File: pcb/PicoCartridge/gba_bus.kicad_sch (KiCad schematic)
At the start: 1 part, among them J1 GameBoy_GamePak_AGB-002

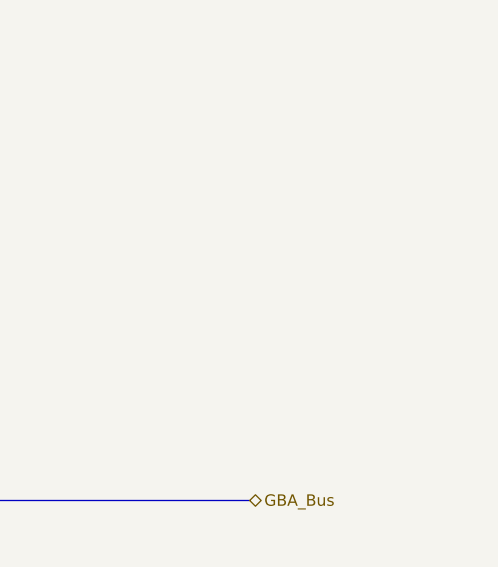
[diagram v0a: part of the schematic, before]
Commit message: Defined additional interfaces
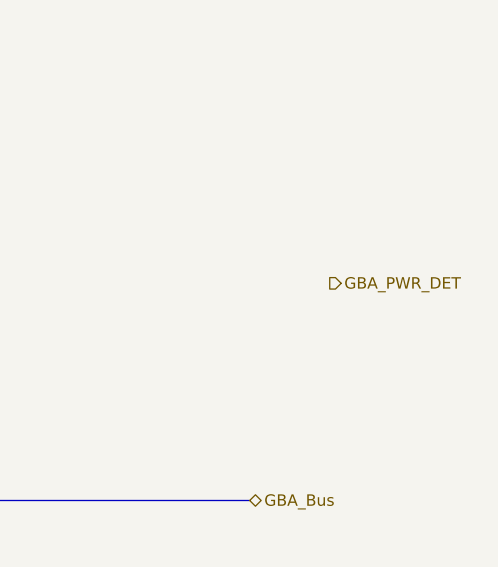
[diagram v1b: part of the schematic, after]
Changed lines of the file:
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@@
+		)
+	)
+	(hierarchical_label "GBA_PWR_DET"
+		(shape output)
+		(at 127 96.52 0)
+		(fields_autoplaced yes)
+		(effects
+			(font
+				(size 1.27 1.27)
+			)
+			(justify left)
 		)
 	)

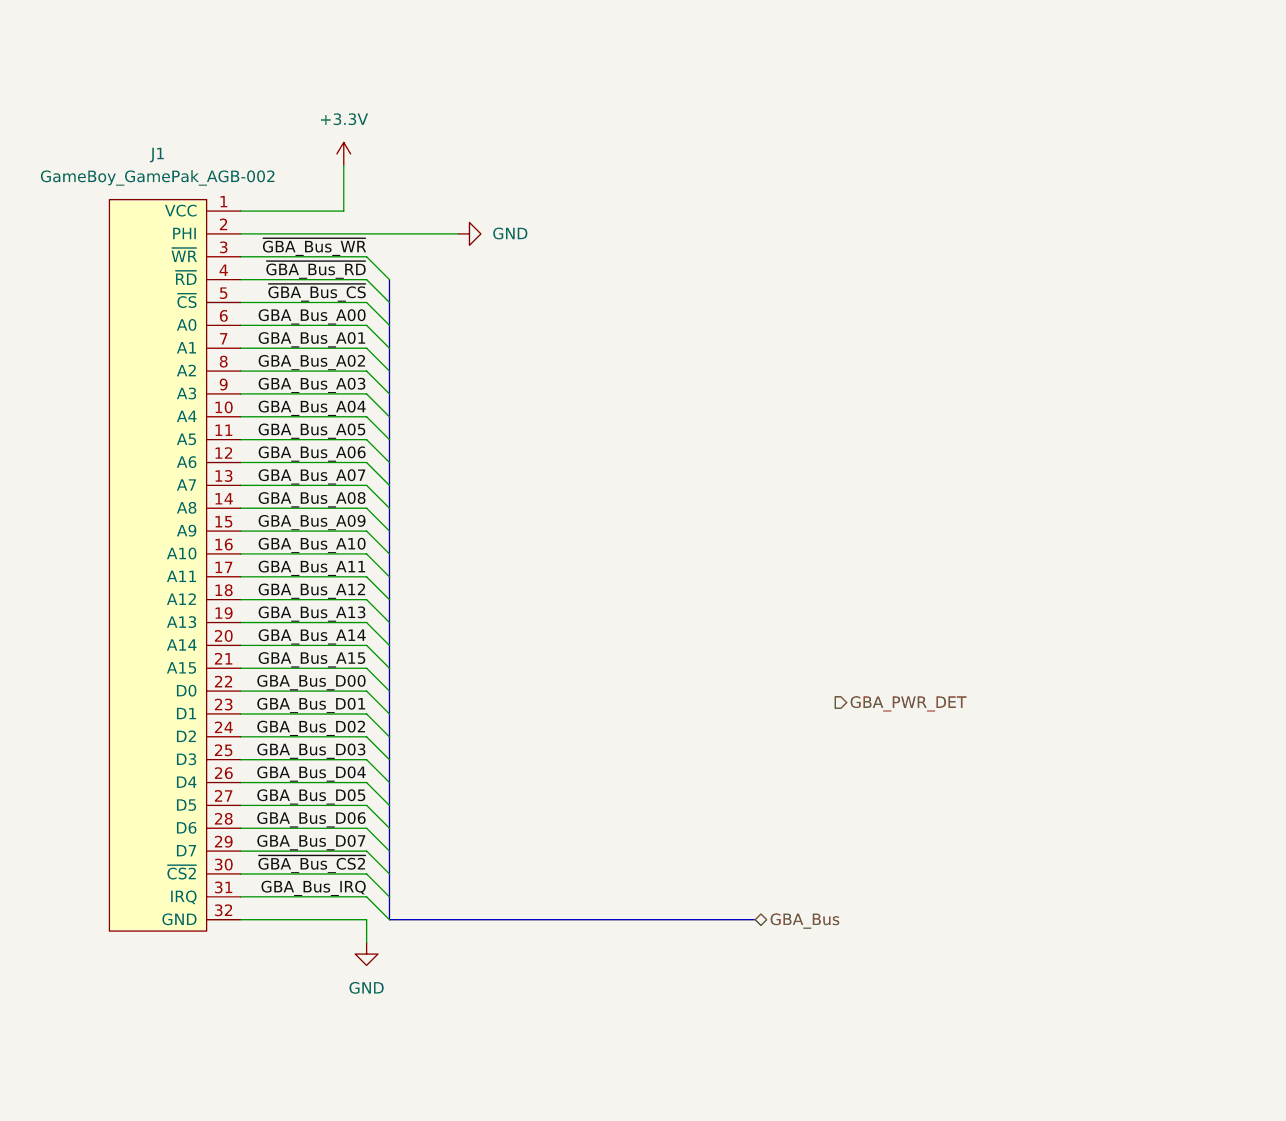
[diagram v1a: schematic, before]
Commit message: Fixed GBA bus internal logic
THe GBA bus is now a correct bus in a sense of kicad
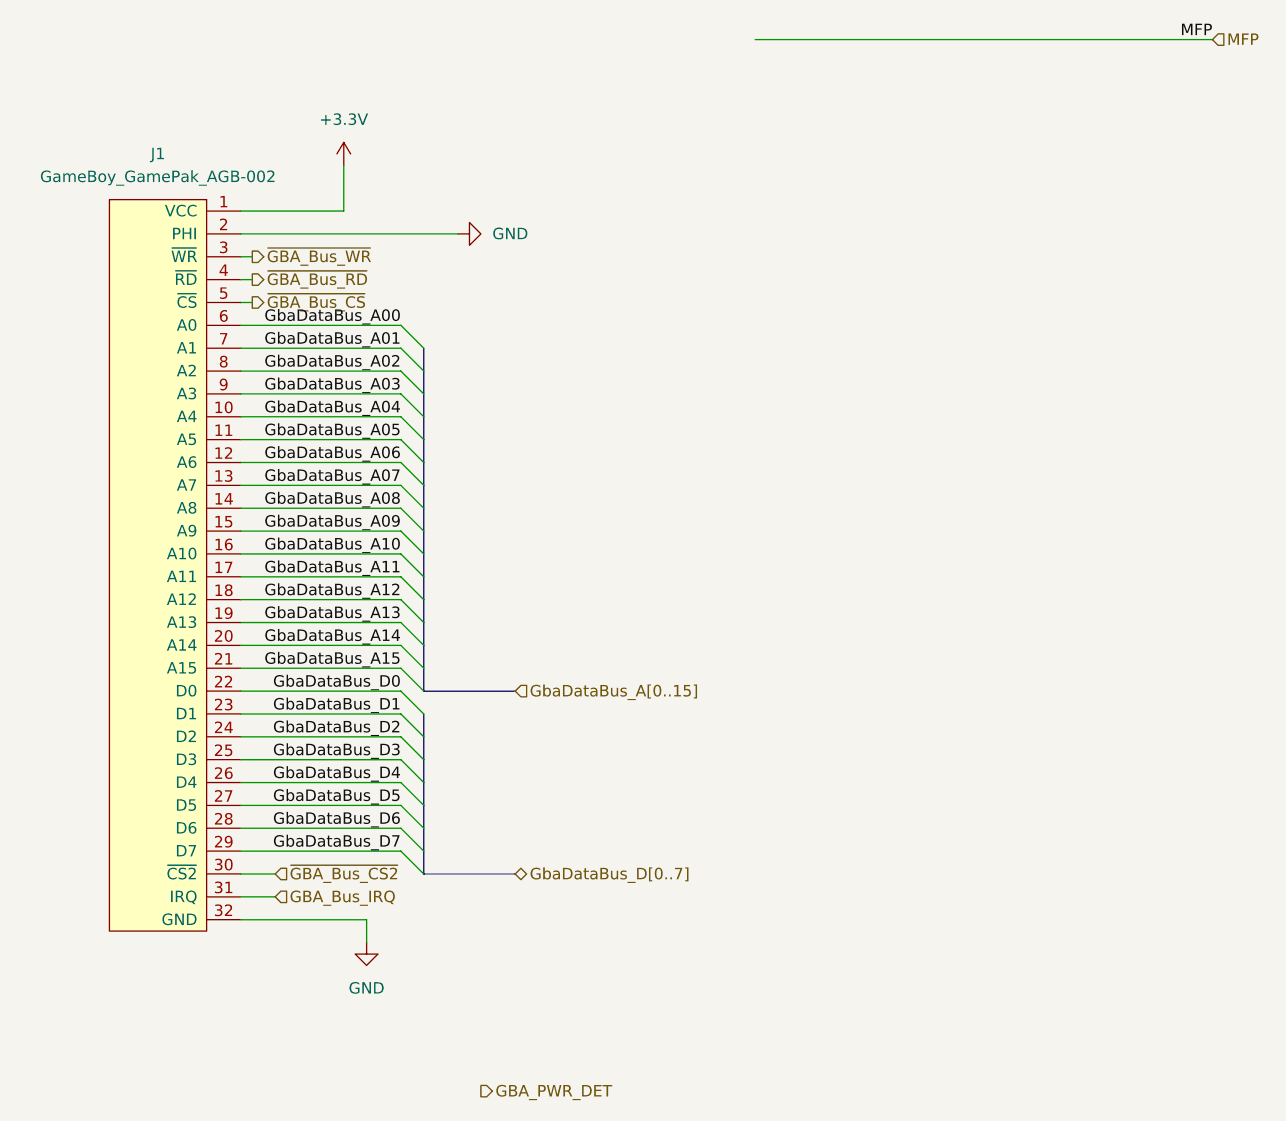
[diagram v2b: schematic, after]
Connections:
- net GBA_Bus_A00 renamed GbaDataBus_A00
- net GBA_Bus_A01 renamed GbaDataBus_A01
- net GBA_Bus_A02 renamed GbaDataBus_A02
- net GBA_Bus_A03 renamed GbaDataBus_A03
- net GBA_Bus_A04 renamed GbaDataBus_A04
- net GBA_Bus_A05 renamed GbaDataBus_A05
- net GBA_Bus_A06 renamed GbaDataBus_A06
- net GBA_Bus_A07 renamed GbaDataBus_A07
- net GBA_Bus_A08 renamed GbaDataBus_A08
- net GBA_Bus_A09 renamed GbaDataBus_A09
- net GBA_Bus_A10 renamed GbaDataBus_A10
- net GBA_Bus_A11 renamed GbaDataBus_A11
- net GBA_Bus_A12 renamed GbaDataBus_A12
- net GBA_Bus_A13 renamed GbaDataBus_A13
- net GBA_Bus_A14 renamed GbaDataBus_A14
- net GBA_Bus_A15 renamed GbaDataBus_A15
- net GBA_Bus_D00 renamed GbaDataBus_D0
- net GBA_Bus_D01 renamed GbaDataBus_D1
- net GBA_Bus_D02 renamed GbaDataBus_D2
- net GBA_Bus_D03 renamed GbaDataBus_D3
- net GBA_Bus_D04 renamed GbaDataBus_D4
- net GBA_Bus_D05 renamed GbaDataBus_D5
- net GBA_Bus_D06 renamed GbaDataBus_D6
- net GBA_Bus_D07 renamed GbaDataBus_D7

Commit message: Upload progress
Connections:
- net GbaDataBus_A00 renamed GbaDataBus_A0
- net GbaDataBus_A01 renamed GbaDataBus_A1
- net GbaDataBus_A02 renamed GbaDataBus_A2
- net GbaDataBus_A03 renamed GbaDataBus_A3
- net GbaDataBus_A04 renamed GbaDataBus_A4
- net GbaDataBus_A05 renamed GbaDataBus_A5
- net GbaDataBus_A06 renamed GbaDataBus_A6
- net GbaDataBus_A07 renamed GbaDataBus_A7
- net GbaDataBus_A08 renamed GbaDataBus_A8
- net GbaDataBus_A09 renamed GbaDataBus_A9
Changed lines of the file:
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@@
 		)
 	)
-	(label "GbaDataBus_A08"
+	(label "GbaDataBus_A8"
 		(at 78.74 74.93 180)
 		(fields_autoplaced yes)
@@
 		)
 	)
-	(label "GbaDataBus_A06"
+	(label "GbaDataBus_A6"
 		(at 78.74 69.85 180)
 		(fields_autoplaced yes)
@@
 		)
 	)
-	(label "GbaDataBus_A01"
+	(label "GbaDataBus_A1"
 		(at 78.74 57.15 180)
 		(fields_autoplaced yes)
@@
 		)
 	)
-	(label "GbaDataBus_A02"
+	(label "GbaDataBus_A2"
 		(at 78.74 59.69 180)
 		(fields_autoplaced yes)
@@
 		)
 	)
-	(label "GbaDataBus_A07"
+	(label "GbaDataBus_A7"
 		(at 78.74 72.39 180)
 		(fields_autoplaced yes)
@@
 		)
 	)
-	(label "GbaDataBus_A04"
+	(label "GbaDataBus_A4"
 		(at 78.74 64.77 180)
 		(fields_autoplaced yes)
@@
 		)
 	)
-	(label "GbaDataBus_A09"
+	(label "GbaDataBus_A9"
 		(at 78.74 77.47 180)
 		(fields_autoplaced yes)
@@
 		)
 	)
-	(label "GbaDataBus_A05"
+	(label "GbaDataBus_A5"
 		(at 78.74 67.31 180)
 		(fields_autoplaced yes)
@@
 		)
 	)
-	(label "GbaDataBus_A00"
+	(label "GbaDataBus_A0"
 		(at 78.74 54.61 180)
 		(fields_autoplaced yes)
@@
 		)
 	)
-	(label "GbaDataBus_A03"
+	(label "GbaDataBus_A3"
 		(at 78.74 62.23 180)
 		(fields_autoplaced yes)
